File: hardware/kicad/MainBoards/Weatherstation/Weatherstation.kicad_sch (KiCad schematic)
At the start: 28 parts, among them J1 Conn_01x02_Pin, J6 USB_C_Receptacle_USB2.0_16P, U1 ESP32-DevKitC, U3 LM3940IMP-3.3/NOPB, U4 24LC32

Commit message: feat(hardware): finalize Weatherstation Rev 0.1
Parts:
- removed C1, C4, C5, C7: 100nF, Capacitor_SMD:C_1206_3216Metric_Pad1.33x1.80mm_HandSolder, symbol Device:C
- removed C2: 10uF, Capacitor_SMD:C_1206_3216Metric_Pad1.33x1.80mm_HandSolder, symbol Device:C
- removed C3: 47uF, Capacitor_Tantalum_SMD:CP_EIA-3528-21_Kemet-B, symbol Device:C_Polarized
- removed C6: 10uF, Capacitor_SMD:CP_Elec_5x5.4, symbol Device:C_Polarized
- removed D1, D2: SS14, Diode_SMD:D_SMA, symbol Diode:SS14
- removed H3, H4, H5, H6: MountingHole, MountingHole:MountingHole_4.3mm_M4, symbol Mechanical:MountingHole
- removed J1: Conn_01x02_Pin, Connector_JST:JST_PH_B2B-PH-K_1x02_P2.00mm_Vertical, symbol Connector:Conn_01x02_Pin
- removed J6: USB_C_Receptacle_USB2.0_16P, Connector_USB:USB_C_Receptacle_GCT_USB4105-xx-A_16P_TopMnt_Horizontal, symbol Connector:USB_C_Receptacle_USB2.0_16P
- removed R5, R6: 5,1kOhm, Resistor_SMD:R_1206_3216Metric_Pad1.30x1.75mm_HandSolder, symbol Device:R
- removed U1: ESP32-DevKitC, PCM_Espressif:ESP32-DevKitC, symbol PCM_Espressif:ESP32-DevKitC
- removed U3: LM3940IMP-3.3/NOPB, Package_TO_SOT_SMD:SOT-223-3_TabPin2, symbol Regulator_Linear:LT1963AxST-3.3
- removed U4: 24LC32, Package_SO:SOIC-8_3.9x4.9mm_P1.27mm, symbol Memory_EEPROM:24LC32
- renumbered R7 to R1, R8 to R2, R9 to R3, R10 to R4
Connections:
- no-connect marks 19 -> 0
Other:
- sheet Module Slot 0 renamed Module Slot A
- added sheet ESP32 (ESP32.kicad_sch)
- added sheet PCB (PCB.kicad_sch)
- added sheet Power (Power.kicad_sch)

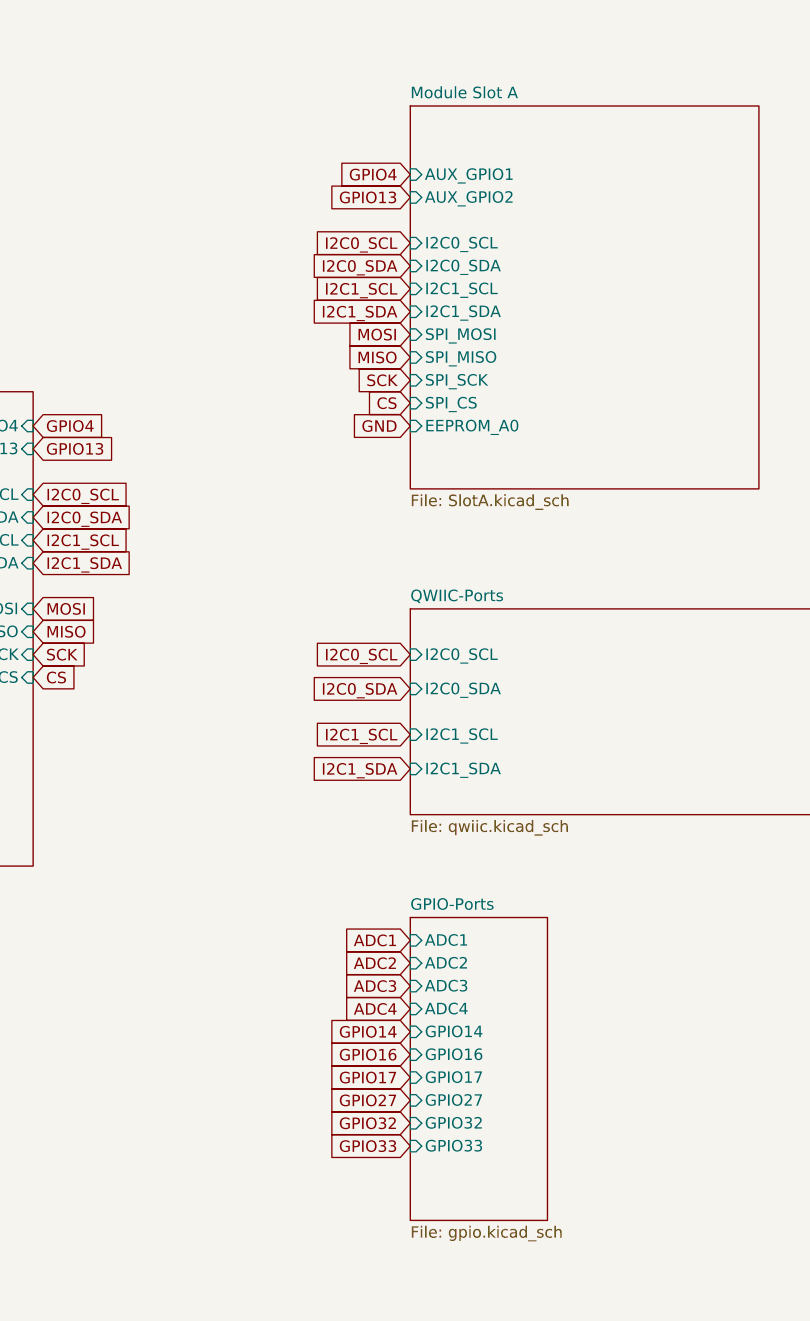
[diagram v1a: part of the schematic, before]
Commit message: hardware(weather): swap slot GPIO4 with GPIO33 for analog input
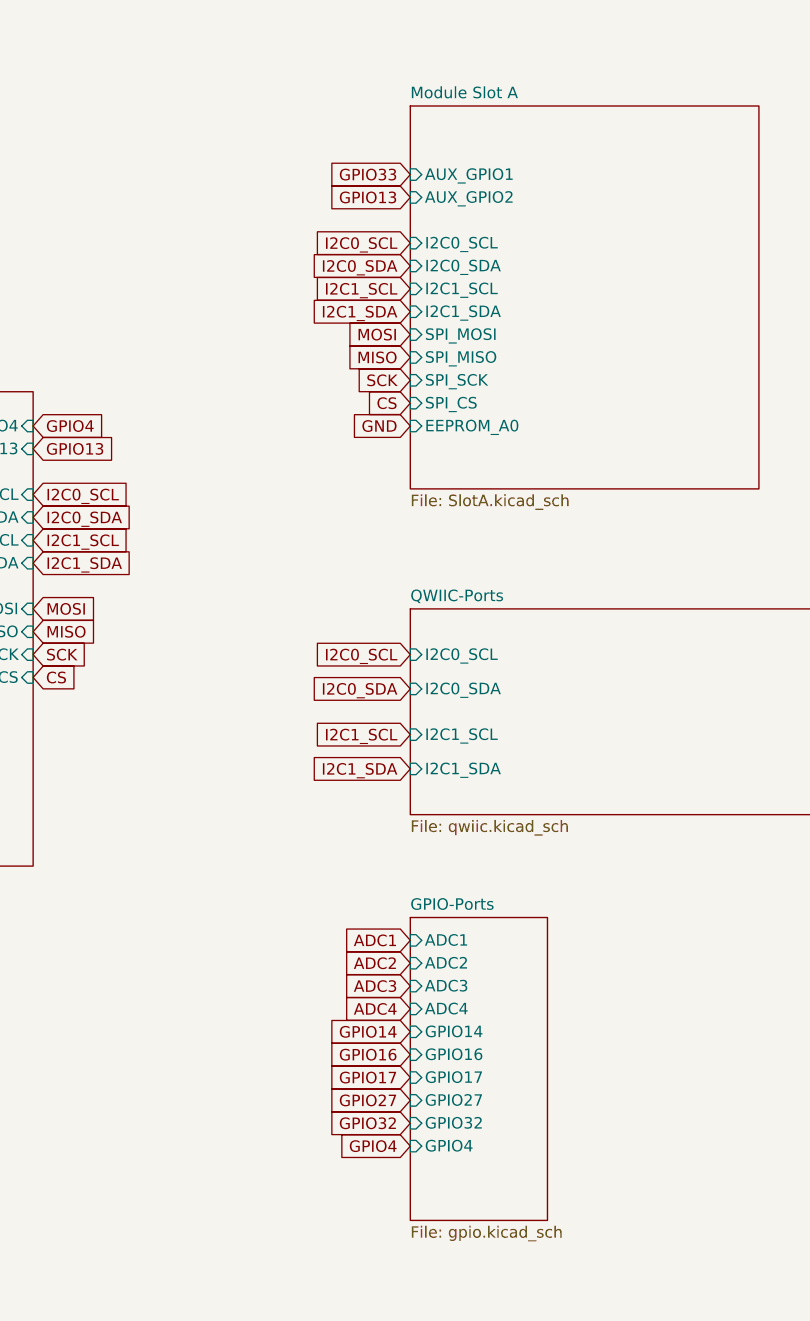
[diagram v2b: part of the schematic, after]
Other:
- sheet GPIO-Ports ports: added GPIO4; removed GPIO33

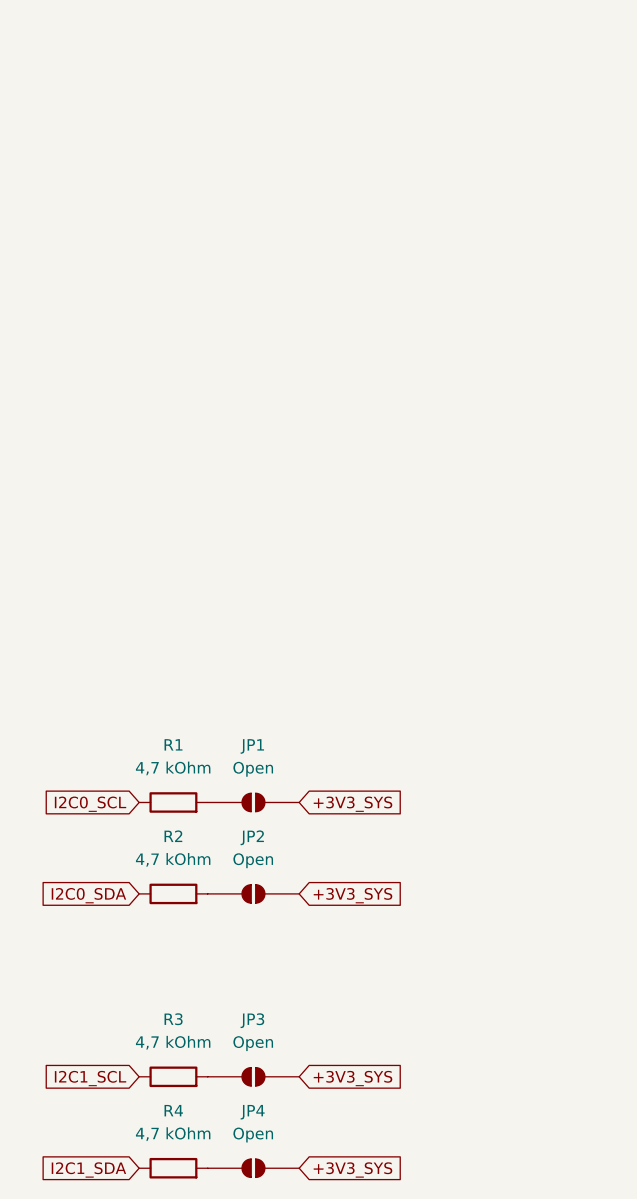
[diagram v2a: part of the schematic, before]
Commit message: Update Mini to 0.9.0 and Weatherstation to 0.3.0
Add TP1 test reference connections isolated through D1/D2 from GND and +3V3_SYS. Replace I2C solder jumpers with removable pull-up jumpers and add C2 for local EEPROM supply decoupling.

Update schematics, PCB layouts, revision markings and KiCad project settings to match the documented hardware revisions.
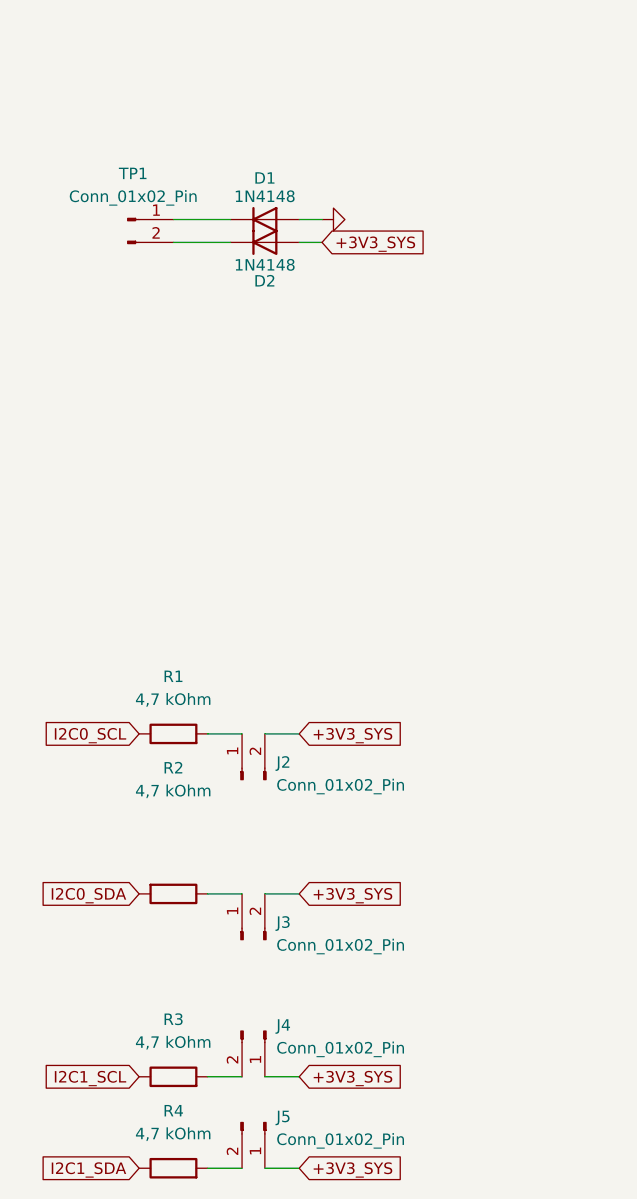
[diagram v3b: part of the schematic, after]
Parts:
- removed JP1, JP2, JP3, JP4: Open, Jumper:SolderJumper-2_P1.3mm_Open_Pad1.0x1.5mm, symbol Jumper:SolderJumper_2_Open
- added D1, D2: 1N4148, Diode_SMD:D_1206_3216Metric_Pad1.42x1.75mm_HandSolder, symbol Device:D
- added J2, J3, J4, J5: Conn_01x02_Pin, Connector_PinHeader_2.54mm:PinHeader_1x02_P2.54mm_Vertical, symbol Connector:Conn_01x02_Pin
- added TP1: Conn_01x02_Pin, Connector_JST:JST_PH_B2B-PH-K_1x02_P2.00mm_Vertical, symbol Connector:Conn_01x02_Pin
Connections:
- net +3V3_SYS: now also D2.2 (A), J2.2 (Pin_2), J3.2 (Pin_2), J4.1 (Pin_1), J5.1 (Pin_1)
- net GND: now also D1.2 (A)
- net I2C0_SDA: now also R2.2; no longer R2.1
- net at R4.2: now also J5.2 (Pin_2)
- net at R3.2: now also J4.2 (Pin_2)
- net at R1.2: now also J2.1 (Pin_1)
- new net: J3.1 (Pin_1), R2.1
- new net: D1.1 (K), TP1.1 (Pin_1)
- new net: D2.1 (K), TP1.2 (Pin_2)
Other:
- moved on the sheet: R1, R2
